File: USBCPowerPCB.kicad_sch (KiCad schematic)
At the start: 5 parts, among them J2 USB_C_Receptacle_USB2.0_16P, J3 5V_OUT, J4 12V_OUT

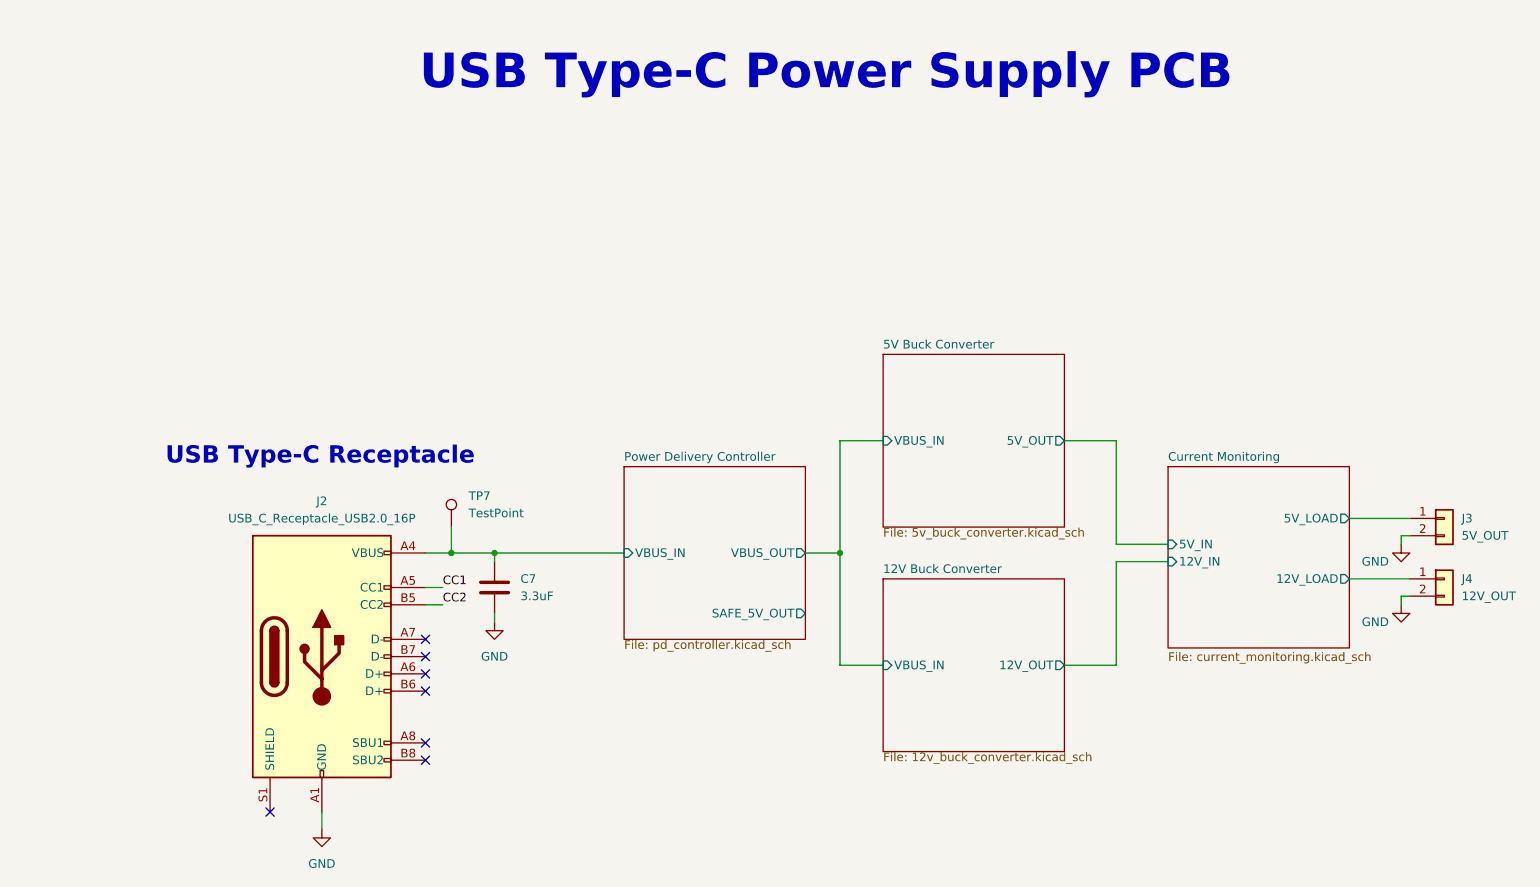
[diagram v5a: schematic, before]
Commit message: changed to 1-channel chip for current sense & fixed ERC
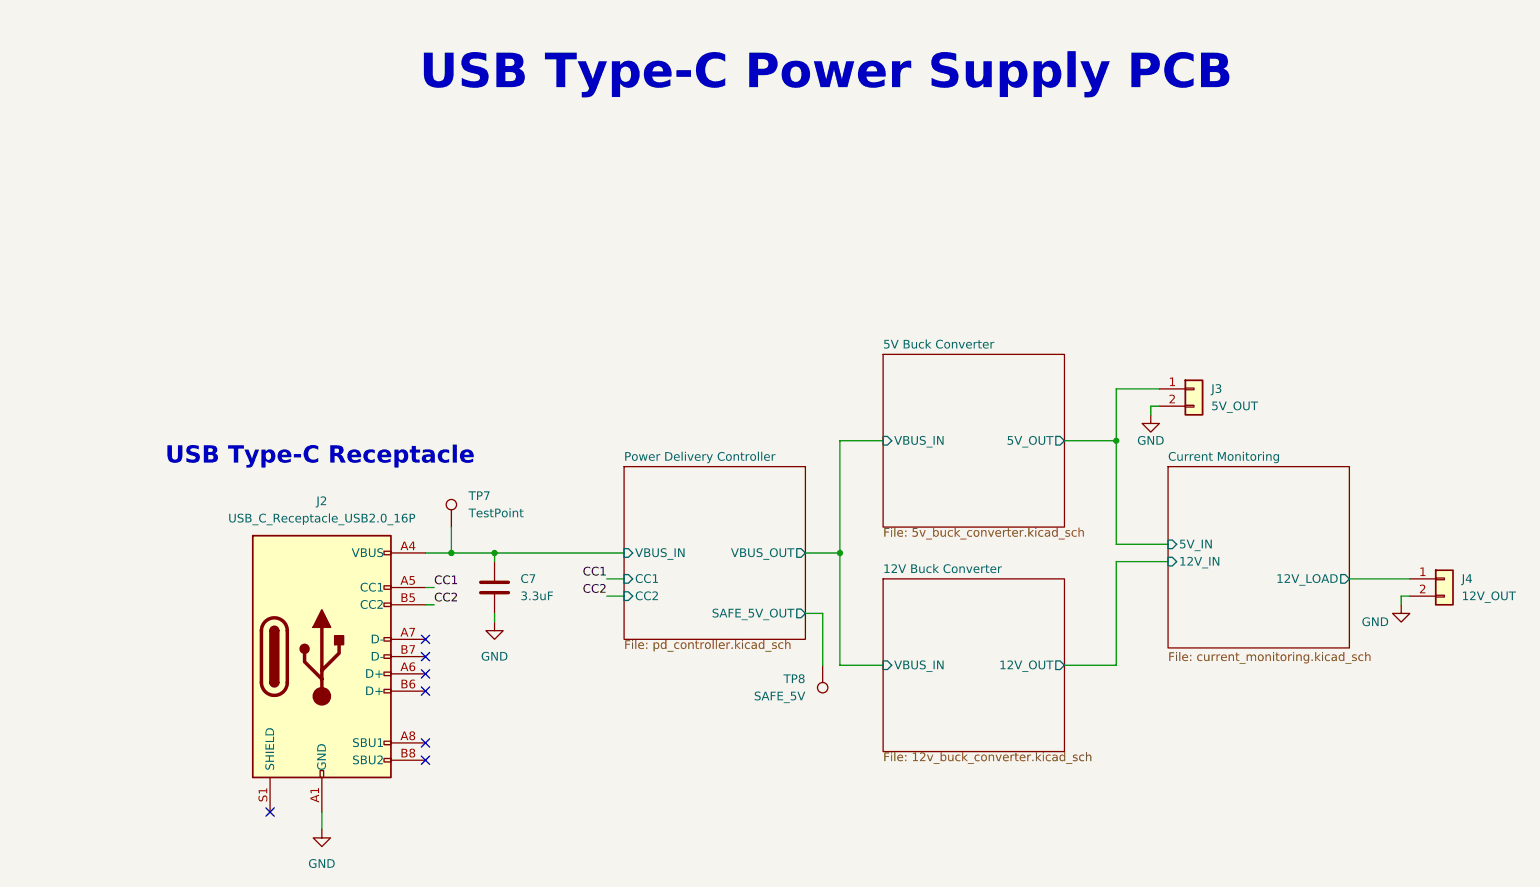
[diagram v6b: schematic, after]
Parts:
- added TP8: SAFE_5V, symbol Connector:TestPoint
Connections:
- net Current Monitoring/5V_LOAD is gone; now on net 5V Buck Converter/5V_OUT: J3.1 (Pin_1)
- net Power Delivery Controller/SAFE_5V_OUT: now also TP8.1
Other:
- sheet Current Monitoring ports: added none; removed 5V_LOAD
- sheet Power Delivery Controller ports: added CC1, CC2; removed none
- moved on the sheet: J3
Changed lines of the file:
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@@
+	)
+	(junction
+		(at 182.88 83.82)
+		(diameter 0)
+		(color 0 0 0 0)
 	)
 	(junction
@@
 	(wire
 		(pts
-			(xy 81.28 105.41) (xy 83.82 105.41)
+			(xy 81.28 105.41) (xy 82.55 105.41)
 		)
 		(stroke
@@
 	(wire
 		(pts
+			(xy 107.95 104.14) (xy 110.49 104.14)
+		)
+		(stroke
+			(width 0)
+			(type default)
+		)
+	)
+	(wire
+		(pts
 			(xy 217.17 104.14) (xy 226.06 104.14)
 		)
@@
 	(wire
 		(pts
-			(xy 81.28 107.95) (xy 83.82 107.95)
+			(xy 81.28 107.95) (xy 82.55 107.95)
 		)
 		(stroke
@@
 	(wire
 		(pts
-			(xy 224.79 99.06) (xy 224.79 97.79)
+			(xy 187.96 80.01) (xy 187.96 78.74)
+		)
+		(stroke
+			(width 0)
+			(type default)
+		)
+	)
+	(wire
+		(pts
+			(xy 189.23 76.2) (xy 182.88 76.2)
 		)
 		(stroke
@@
 	(wire
 		(pts
+			(xy 137.16 109.22) (xy 139.7 109.22)
+		)
+		(stroke
+			(width 0)
+			(type default)
+		)
+	)
+	(wire
+		(pts
 			(xy 142.24 116.84) (xy 142.24 100.33)
 		)
@@
 	(wire
 		(pts
-			(xy 217.17 95.25) (xy 226.06 95.25)
+			(xy 182.88 76.2) (xy 182.88 83.82)
 		)
 		(stroke
@@
 	(wire
 		(pts
-			(xy 224.79 97.79) (xy 226.06 97.79)
+			(xy 187.96 78.74) (xy 189.23 78.74)
 		)
 		(stroke
@@
 	(wire
 		(pts
+			(xy 107.95 106.68) (xy 110.49 106.68)
+		)
+		(stroke
+			(width 0)
+			(type default)
+		)
+	)
+	(wire
+		(pts
 			(xy 91.44 100.33) (xy 91.44 101.6)
+		)
+		(stroke
+			(width 0)
+			(type default)
+		)
+	)
+	(wire
+		(pts
+			(xy 139.7 109.22) (xy 139.7 116.84)
 		)
 		(stroke
@@
 	)
 	(label "CC2"
-		(at 83.82 107.95 0)
+		(at 82.55 107.95 0)
 		(fields_autoplaced yes)
 		(effects
@@
 		)
 	)
-	(label "CC1"
-		(at 83.82 105.41 0)
+	(label "CC2"
+		(at 107.95 106.68 180)
 		(fields_autoplaced yes)
 		(effects
@@
 				(size 1.27 1.27)
 			)
+			(justify right bottom)
+		)
+	)
+	(label "CC1"
+		(at 82.55 105.41 0)
+		(fields_autoplaced yes)
+		(effects
+			(font
+				(size 1.27 1.27)
+			)
 			(justify left bottom)
+		)
+	)
+	(label "CC1"
+		(at 107.95 104.14 180)
+		(fields_autoplaced yes)
+		(effects
+			(font
+				(size 1.27 1.27)
+			)
+			(justify right bottom)
 		)
 	)
 	(symbol
 		(lib_id "Connector_Generic:Conn_01x02")
-		(at 231.14 95.25 0)
+		(at 194.31 76.2 0)
 		(unit 1)
 		(exclude_from_sim no)
@@
 		(fields_autoplaced yes)
 		(property "Reference" "J3"
-			(at 233.68 95.2499 0)
+			(at 196.85 76.1999 0)
 			(effects
 				(font
@@
 		)
 		(property "Value" "5V_OUT"
-			(at 233.68 97.7899 0)
+			(at 196.85 78.7399 0)
 			(effects
 				(font
@@
 		)
 		(property "Footprint" ""
-			(at 231.14 95.25 0)
+			(at 194.31 76.2 0)
 			(effects
 				(font
@@
 		)
 		(property "Datasheet" "~"
-			(at 231.14 95.25 0)
+			(at 194.31 76.2 0)
 			(effects
 				(font
@@
 		)
 		(property "Description" "Generic connector, single row, 01x02, script generated (kicad-library-utils/schlib/autogen/connector/)"
-			(at 231.14 95.25 0)
+			(at 194.31 76.2 0)
 			(effects
 				(font
@@
 	(symbol
 		(lib_id "power:GND")
-		(at 224.79 99.06 0)
+		(at 187.96 80.01 0)
 		(unit 1)
 		(exclude_from_sim no)
@@
 		(dnp no)
 		(property "Reference" "#PWR050"
-			(at 224.79 105.41 0)
+			(at 187.96 86.36 0)
 			(effects
 				(font
@@
 		)
 		(property "Value" "GND"
-			(at 220.98 101.6 0)
+			(at 187.96 83.82 0)
 			(effects
 				(font
@@
 		)
 		(property "Footprint" ""
-			(at 224.79 99.06 0)
+			(at 187.96 80.01 0)
 			(effects
 				(font
@@
 		)
 		(property "Datasheet" ""
-			(at 224.79 99.06 0)
+			(at 187.96 80.01 0)
 			(effects
 				(font
@@
 		)
 		(property "Description" "Power symbol creates a global label with name \"GND\" , ground"
-			(at 224.79 99.06 0)
+			(at 187.96 80.01 0)
 			(effects
 				(font
@@
 	)
 	(symbol
+		(lib_id "Connector:TestPoint")
+		(at 139.7 116.84 0)
+		(mirror x)
+		(unit 1)
+		(exclude_from_sim no)
+		(in_bom yes)
+		(on_board yes)
+		(dnp no)
+		(property "Reference" "TP8"
+			(at 137.16 118.8719 0)
+			(effects
+				(font
+					(size 1.27 1.27)
+				)
+				(justify right)
+			)
+		)
+		(property "Value" "SAFE_5V"
+			(at 137.16 121.4119 0)
+			(effects
+				(font
+					(size 1.27 1.27)
+				)
+				(justify right)
+			)
+		)
+		(property "Footprint" ""
+			(at 144.78 116.84 0)
+			(effects
+				(font
+					(size 1.27 1.27)
+				)
+				(hide yes)
+			)
+		)
+		(property "Datasheet" "~"
+			(at 144.78 116.84 0)
+			(effects
+				(font
+					(size 1.27 1.27)
+				)
+				(hide yes)
+			)
+		)
+		(property "Description" "test point"
+			(at 139.7 116.84 0)
+			(effects
+				(font
+					(size 1.27 1.27)
+				)
+				(hide yes)
+			)
+		)
+		(pin "1"
+		)
+		(instances
+			(project ""
+				(path "/f58400c5-df4b-4929-8d2b-33c0fe23fcd9"
+					(reference "TP8")
+					(unit 1)
+				)
+			)
+		)
+	)
+	(symbol
 		(lib_id "Connector:USB_C_Receptacle_USB2.0_16P")
 		(at 66.04 115.57 0)
@@
 			)
 		)
-		(pin "5V_LOAD" output
-			(at 217.17 95.25 0)
-			(effects
-				(font
-					(size 1.27 1.27)
-				)
-				(justify right)
-			)
-		)
 		(instances
 			(project "USBCPowerPCB"
@@
 			)
 		)
+		(pin "CC1" input
+			(at 110.49 104.14 180)
+			(effects
+				(font
+					(size 1.27 1.27)
+				)
+				(justify left)
+			)
+		)
+		(pin "CC2" input
+			(at 110.49 106.68 180)
+			(effects
+				(font
+					(size 1.27 1.27)
+				)
+				(justify left)
+			)
+		)

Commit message: updated with some new footprints (have yet to finish footprint assignment; also need to switch out inductor for 5V buck)
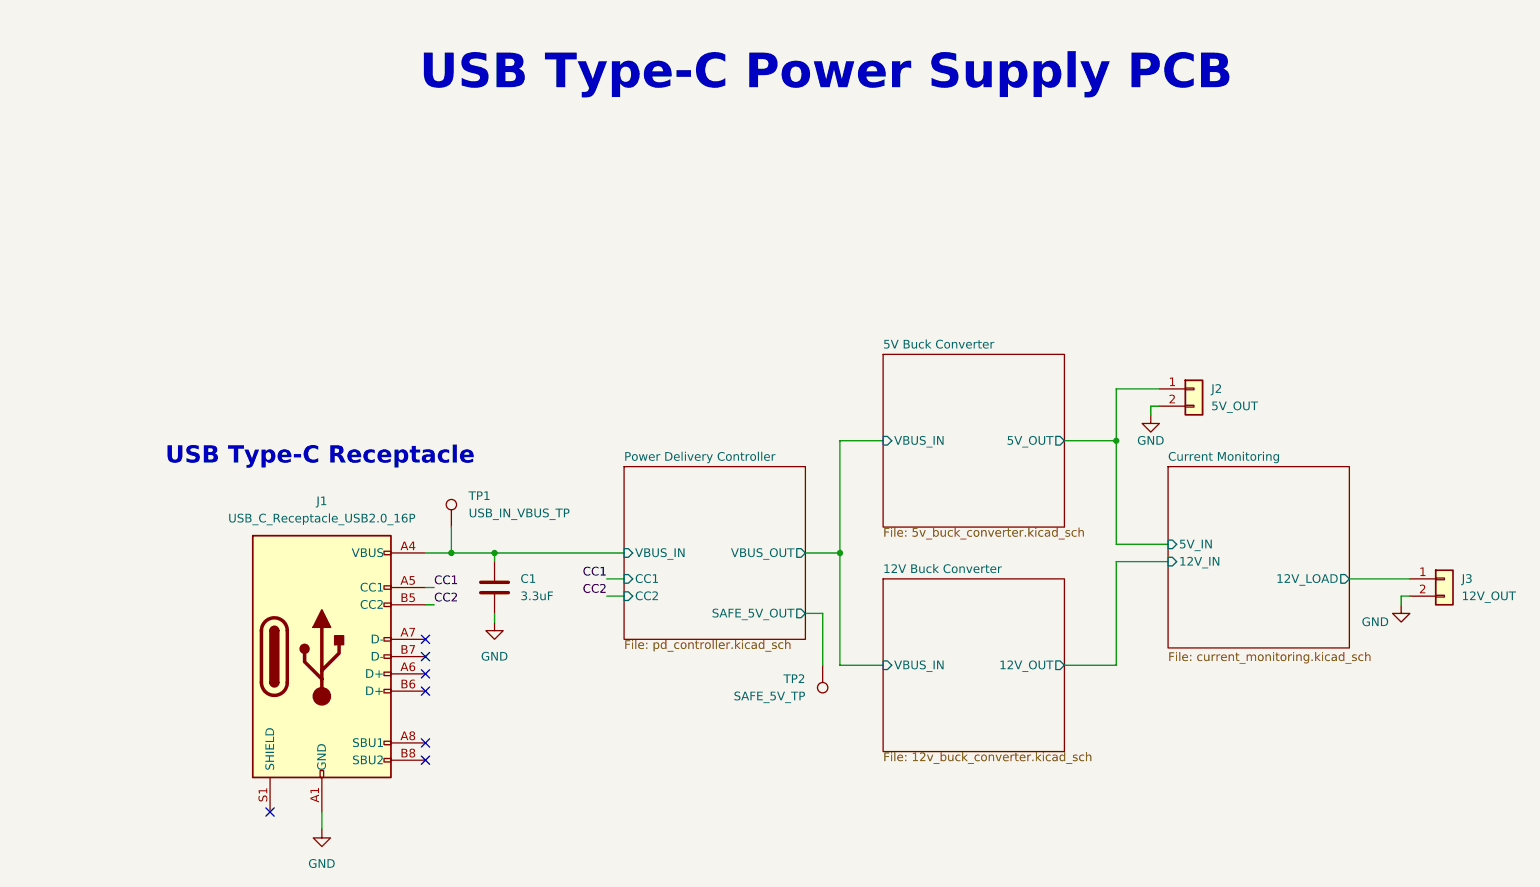
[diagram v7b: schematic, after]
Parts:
- C1: renamed from C7; footprint (none) -> Capacitor_SMD:C_0805_2012Metric
- TP1: renamed from TP7; value TestPoint -> USB_IN_VBUS_TP; footprint (none) -> TestPoint:TestPoint_Pad_D2.5mm
- TP2: renamed from TP8; value SAFE_5V -> SAFE_5V_TP; footprint (none) -> TestPoint:TestPoint_Pad_D2.5mm
- renumbered J2 to J1, J3 to J2, J4 to J3

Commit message: changed 5v buck to TPS56A37
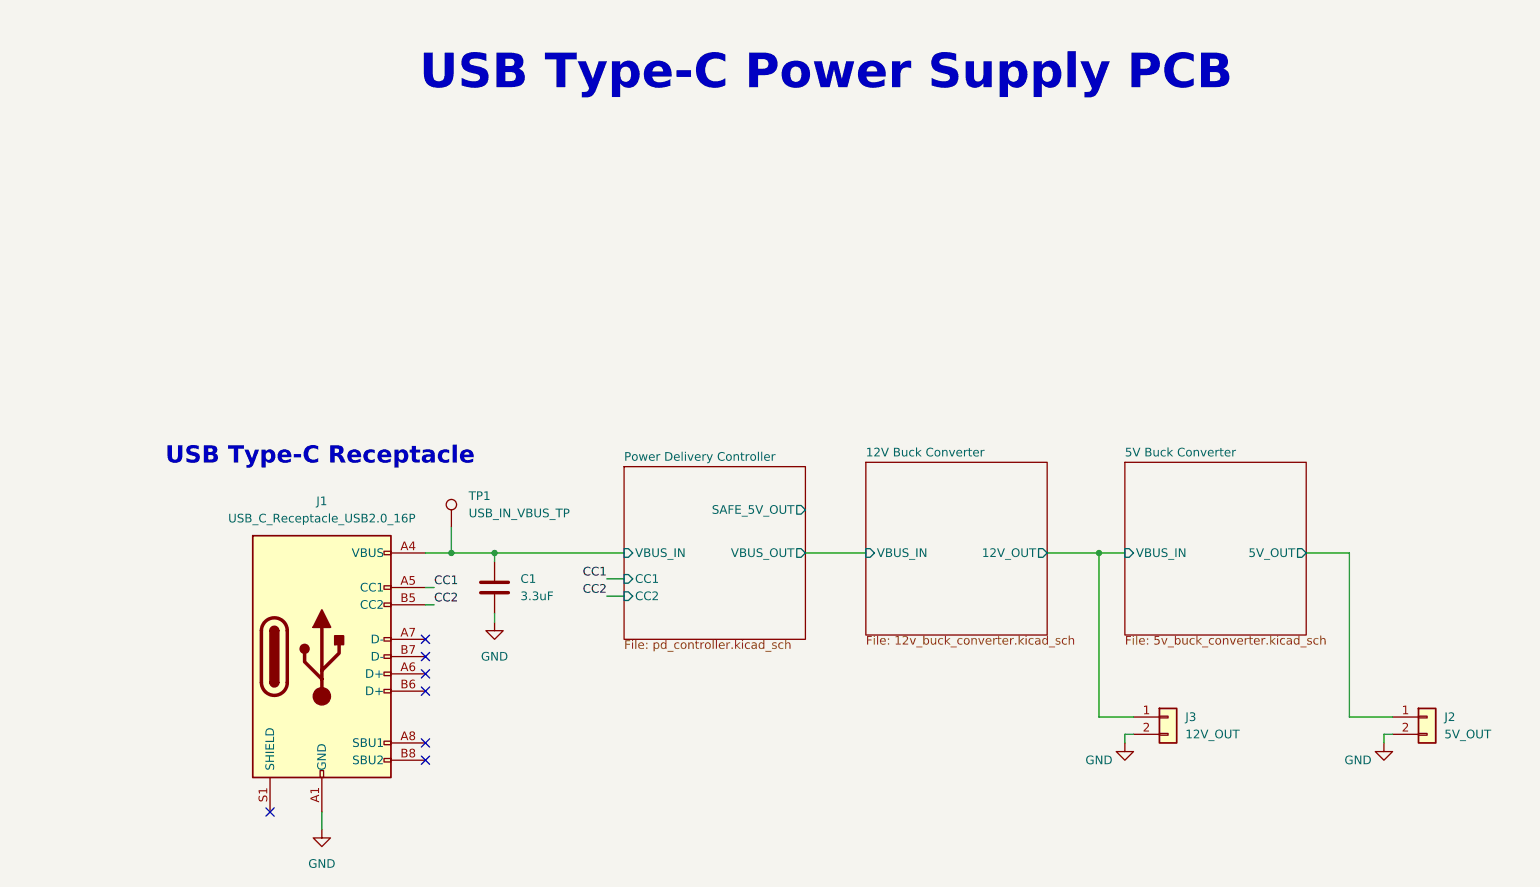
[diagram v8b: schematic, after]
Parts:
- removed TP2: SAFE_5V_TP, TestPoint:TestPoint_Pad_D2.5mm, symbol Connector:TestPoint
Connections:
- net Current Monitoring/12V_LOAD is gone; now on net 12V Buck Converter/12V_OUT: J3.1 (Pin_1)
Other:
- removed sheet Current Monitoring
- moved on the sheet: J3
